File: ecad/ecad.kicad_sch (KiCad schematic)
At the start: 9 parts, among them J1 Raspberry_Pi_2_3, Q1 BC547

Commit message: update schematic
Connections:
- net RFID_IRQ: now reaches J1.18 (GPIO24)
- net RFID_IRQ: now also U4.5 (IRQ)
- net ~{RFID_RST}: now reaches J1.22 (GPIO25)
- net ~{RFID_RST}: now also U4.7 (RST)
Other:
- note removed: "IRQ and RST are connected to the Pi. Need to look it up."
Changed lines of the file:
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@@
   (no_connect (at 207.01 74.93))
   (no_connect (at 54.61 101.6))
+  (wire (pts (xy 115.57 123.19) (xy 116.84 123.19))
+    (stroke (width 0) (type default))
+  )
   (wire (pts (xy 62.23 127) (xy 62.23 104.14))
     (stroke (width 0) (type default))
@@
     (stroke (width 0) (type default))
   )
+  (wire (pts (xy 115.57 128.27) (xy 116.84 128.27))
+    (stroke (width 0) (type default))
+  )
   (wire (pts (xy 44.45 40.64) (xy 48.26 40.64))
     (stroke (width 0) (type default))
@@
     (stroke (width 0) (type default))
   )
+  (wire (pts (xy 110.49 124.46) (xy 115.57 124.46))
+    (stroke (width 0) (type default))
+  )
   (wire (pts (xy 85.09 81.28) (xy 85.09 78.74))
     (stroke (width 0) (type default))
@@
     (stroke (width 0) (type default))
   )
+  (wire (pts (xy 27.94 104.14) (xy 27.94 102.87))
+    (stroke (width 0) (type default))
+  )
   (wire (pts (xy 91.44 151.13) (xy 91.44 157.48))
     (stroke (width 0) (type default))
@@
     (stroke (width 0) (type default))
   )
+  (wire (pts (xy 27.94 102.87) (xy 26.67 102.87))
+    (stroke (width 0) (type default))
+  )
+  (wire (pts (xy 115.57 127) (xy 110.49 127))
+    (stroke (width 0) (type default))
+  )
   (wire (pts (xy 196.85 69.85) (xy 196.85 74.93))
     (stroke (width 0) (type default))
@@
     (stroke (width 0) (type default))
   )
+  (wire (pts (xy 36.83 104.14) (xy 27.94 104.14))
+    (stroke (width 0) (type default))
+  )
   (wire (pts (xy 201.93 68.58) (xy 201.93 67.31))
     (stroke (width 0) (type default))
@@
     (stroke (width 0) (type default))
   )
+  (wire (pts (xy 26.67 106.68) (xy 36.83 106.68))
+    (stroke (width 0) (type default))
+  )
   (wire (pts (xy 48.26 40.64) (xy 48.26 44.45))
     (stroke (width 0) (type default))
   )
+  (wire (pts (xy 115.57 128.27) (xy 115.57 127))
+    (stroke (width 0) (type default))
+  )
   (wire (pts (xy 62.23 40.64) (xy 66.04 40.64))
     (stroke (width 0) (type default))
@@
     (stroke (width 0) (type default))
   )
+  (wire (pts (xy 115.57 124.46) (xy 115.57 123.19))
+    (stroke (width 0) (type default))
+  )
   (wire (pts (xy 30.48 95.25) (xy 30.48 101.6))
     (stroke (width 0) (type default))
@@
   (wire (pts (xy 57.15 109.22) (xy 54.61 109.22))
     (stroke (width 0) (type default))
-  )
-  (text "IRQ and RST are\nconnected to the Pi.\nNeed to look it up."
-    (at 13.97 107.95 0)
-    (effects (font (size 1.27 1.27)) (justify left bottom))
   )
   (text "Probably best to tie these together along\nthe signal path/close to the amp!"
@@
     (effects (font (size 1.27 1.27)) (justify left bottom))
   )
+  (global_label "RFID_IRQ" (shape input) (at 26.67 102.87 180) (fields_autoplaced)
+    (effects (font (size 1.27 1.27)) (justify right))
+    (property "Intersheetrefs" "${INTERSHEET_REFS}" (at 15.2785 102.87 0)
+      (effects (font (size 1.27 1.27)) (justify right) hide)
+    )
+  )
   (global_label "AudioGND" (shape input) (at 227.33 140.97 0) (fields_autoplaced)
     (effects (font (size 1.27 1.27)) (justify left))
@@
     )
   )
+  (global_label "RFID_IRQ" (shape input) (at 116.84 123.19 0) (fields_autoplaced)
+    (effects (font (size 1.27 1.27)) (justify left))
+    (property "Intersheetrefs" "${INTERSHEET_REFS}" (at 128.2315 123.19 0)
+      (effects (font (size 1.27 1.27)) (justify left) hide)
+    )
+  )
+  (global_label "~{RFID_RST}" (shape input) (at 116.84 128.27 0) (fields_autoplaced)
+    (effects (font (size 1.27 1.27)) (justify left))
+    (property "Intersheetrefs" "${INTERSHEET_REFS}" (at 128.4733 128.27 0)
+      (effects (font (size 1.27 1.27)) (justify left) hide)
+    )
+  )
+  (global_label "~{RFID_RST}" (shape input) (at 26.67 106.68 180) (fields_autoplaced)
+    (effects (font (size 1.27 1.27)) (justify right))
+    (property "Intersheetrefs" "${INTERSHEET_REFS}" (at 15.0367 106.68 0)
+      (effects (font (size 1.27 1.27)) (justify right) hide)
+    )
+  )

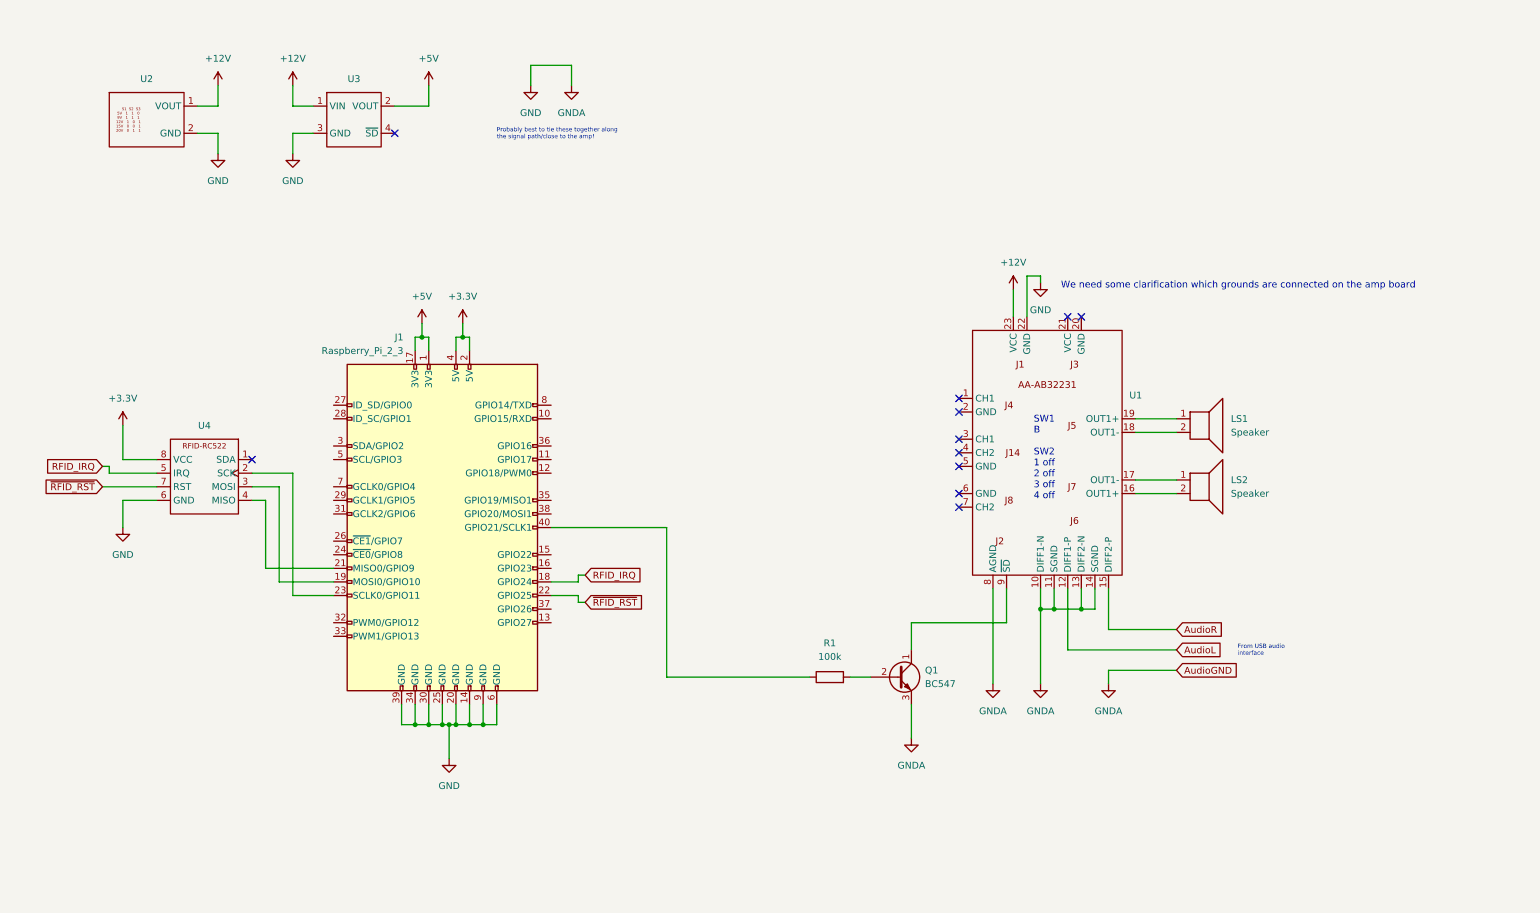
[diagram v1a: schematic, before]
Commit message: pi softoff, new amp power control
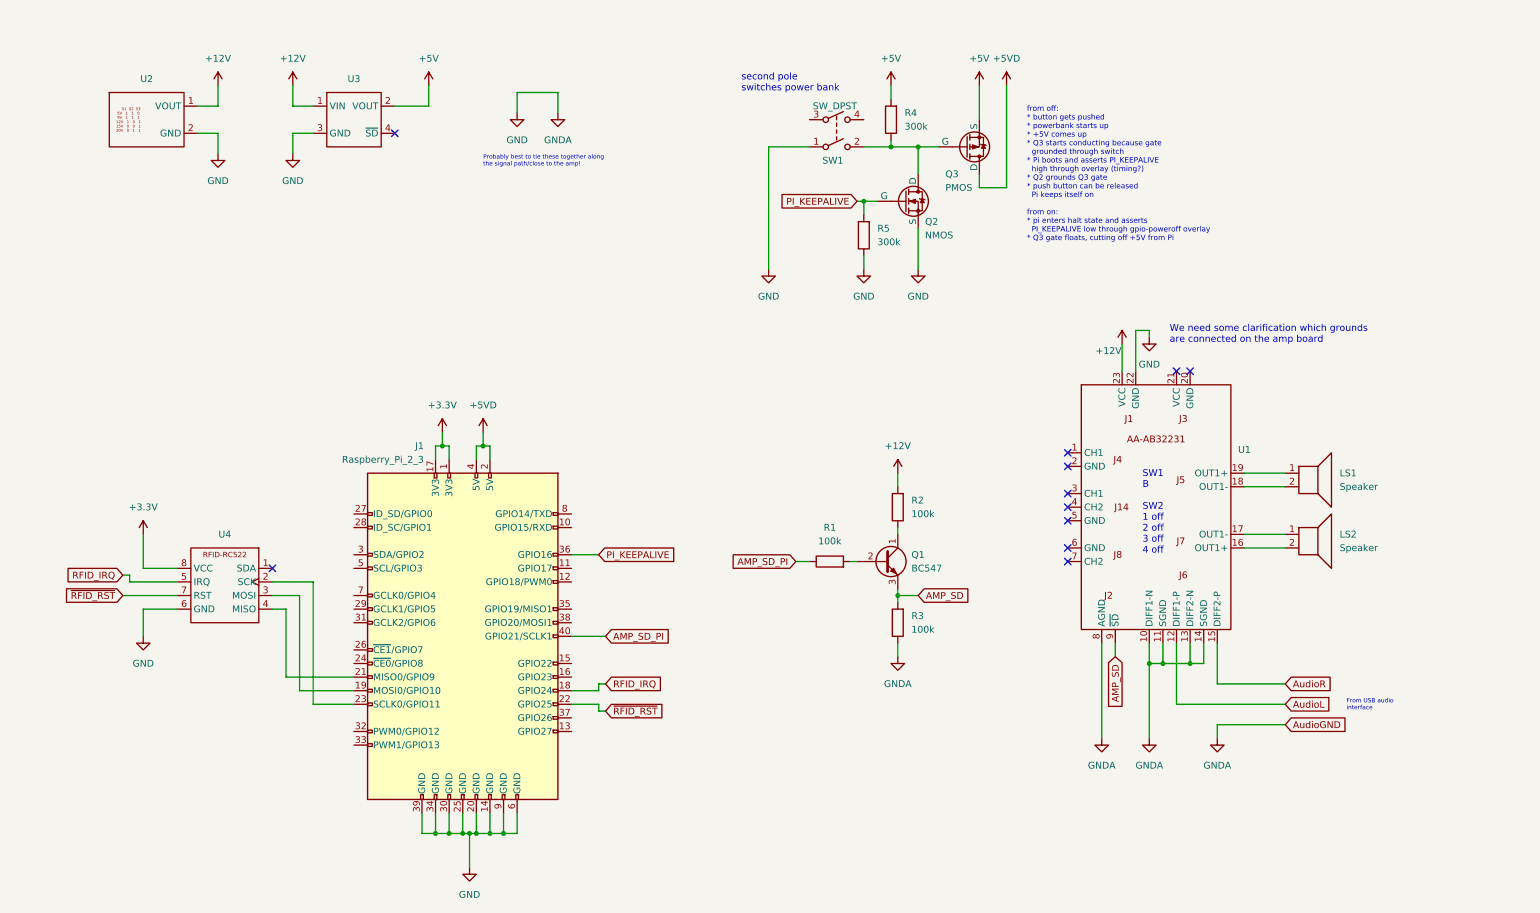
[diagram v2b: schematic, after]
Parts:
- added Q2: NMOS, symbol Simulation_SPICE:NMOS
- added Q3: PMOS, symbol Simulation_SPICE:PMOS
- added R2, R3: 100k, symbol Device:R
- added R4, R5: 300k, symbol Device:R
- added SW1: SW_DPST, symbol Switch:SW_DPST
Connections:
- net +12V: now also R2.2
- net +3.3V: now also J1.1 (3V3), J1.17 (3V3); no longer J1.2 (5V), J1.4 (5V)
- net +5V: now also Q3.3 (S), R4.2; no longer J1.1 (3V3), J1.17 (3V3)
- net GND: now also Q2.3 (S), R3.1, R5.1, SW1.1; no longer Q1.3 (E)
- net PI_KEEPALIVE: now reaches J1.36 (GPIO16)
- net PI_KEEPALIVE: now also Q2.2 (G), R5.2
- net AMP_SD_PI: now reaches J1.40 (GPIO21/SCLK1), R1.1
- net at Q1.1 (C): now also R2.1; no longer U1.9 (~{SD})
- new net: Q2.1 (D), Q3.2 (G), R4.1, SW1.2
- new net +5VD: J1.2 (5V), J1.4 (5V), Q3.1 (D)
- new net AMP_SD: Q1.3 (E), R3.2, U1.9 (~{SD})
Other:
- note added: "from off: * button gets pushed * powerbank starts up * +5V comes up * Q3 starts conducting because gate grounded through switch * Pi boots and asserts PI_KEEPALIVE high through overlay (timing?) * Q2 grounds Q3 gate * push button can be released Pi keeps itself on from on: * pi enters halt state and asserts PI_KEEPALIVE low through gpio-poweroff overlay * Q3 gate floats, cutting off +5V from Pi"
- note added: "second pole switches power bank"
- moved on the sheet: J1, LS1, LS2, Q1, R1, U1, U4

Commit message: updated amp control, more notes
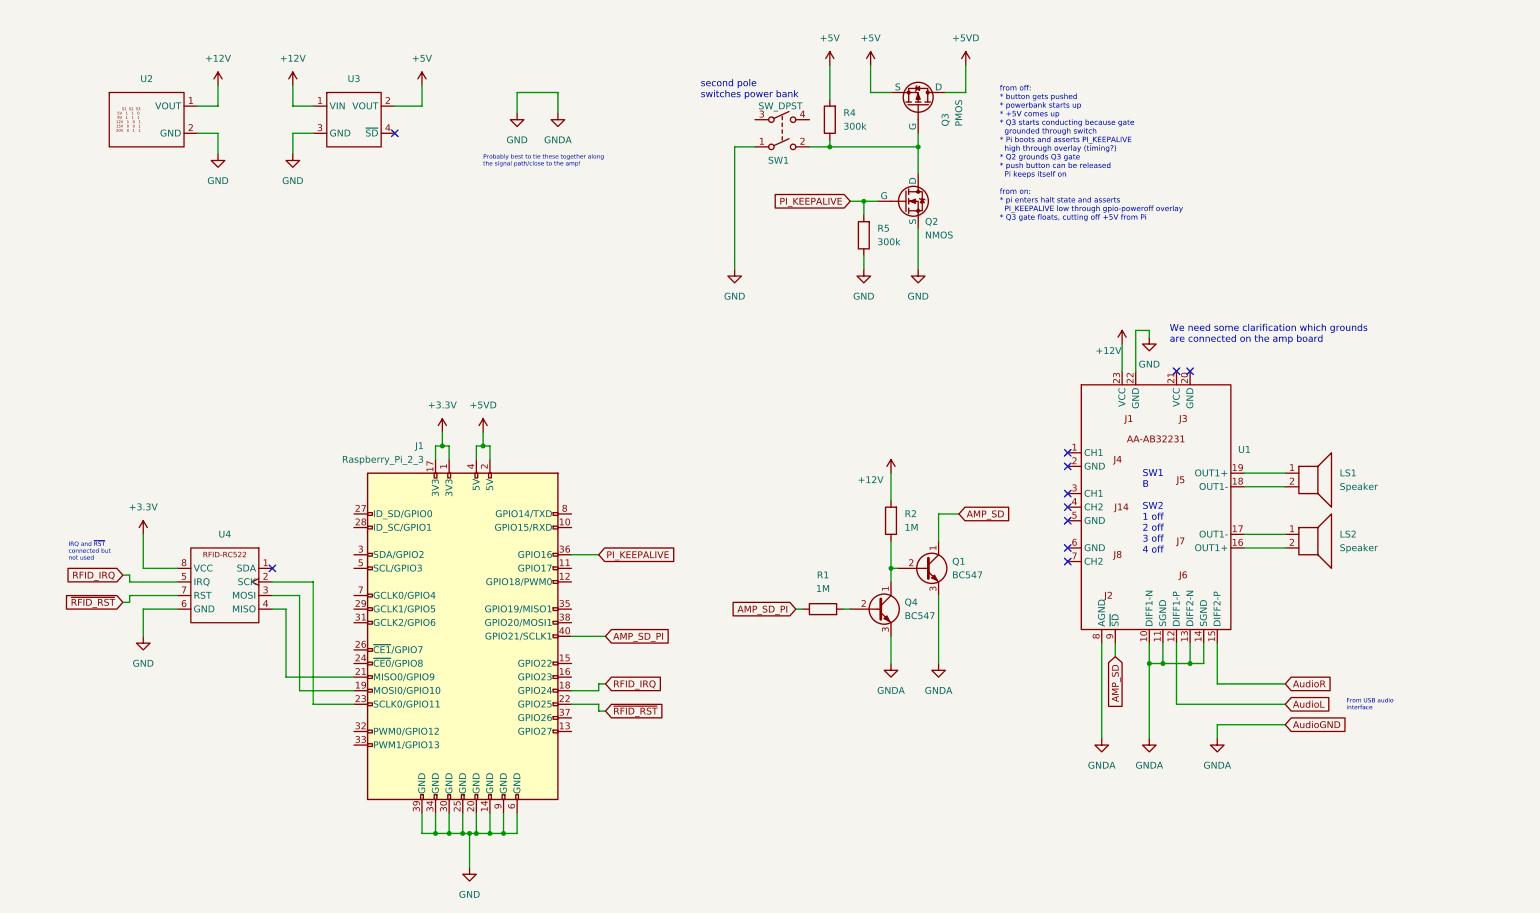
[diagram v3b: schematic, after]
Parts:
- removed R3: 100k, symbol Device:R
- added Q4: BC547, Package_TO_SOT_THT:TO-92_Inline, symbol Transistor_BJT:BC547
- R1, R2: value 100k -> 1M
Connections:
- net AMP_SD: now also Q1.1 (C); no longer Q1.3 (E)
- net GND: now also Q1.3 (E), Q4.3 (E)
- net at R2.1: now also Q1.2 (B), Q4.1 (C); no longer Q1.1 (C)
- net at R1.2: now also Q4.2 (B); no longer Q1.2 (B)
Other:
- note added: "IRQ and ~{RST} connected but not used"
- moved on the sheet: Q1, Q3, R1, R2, R4, SW1

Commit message: refine power management
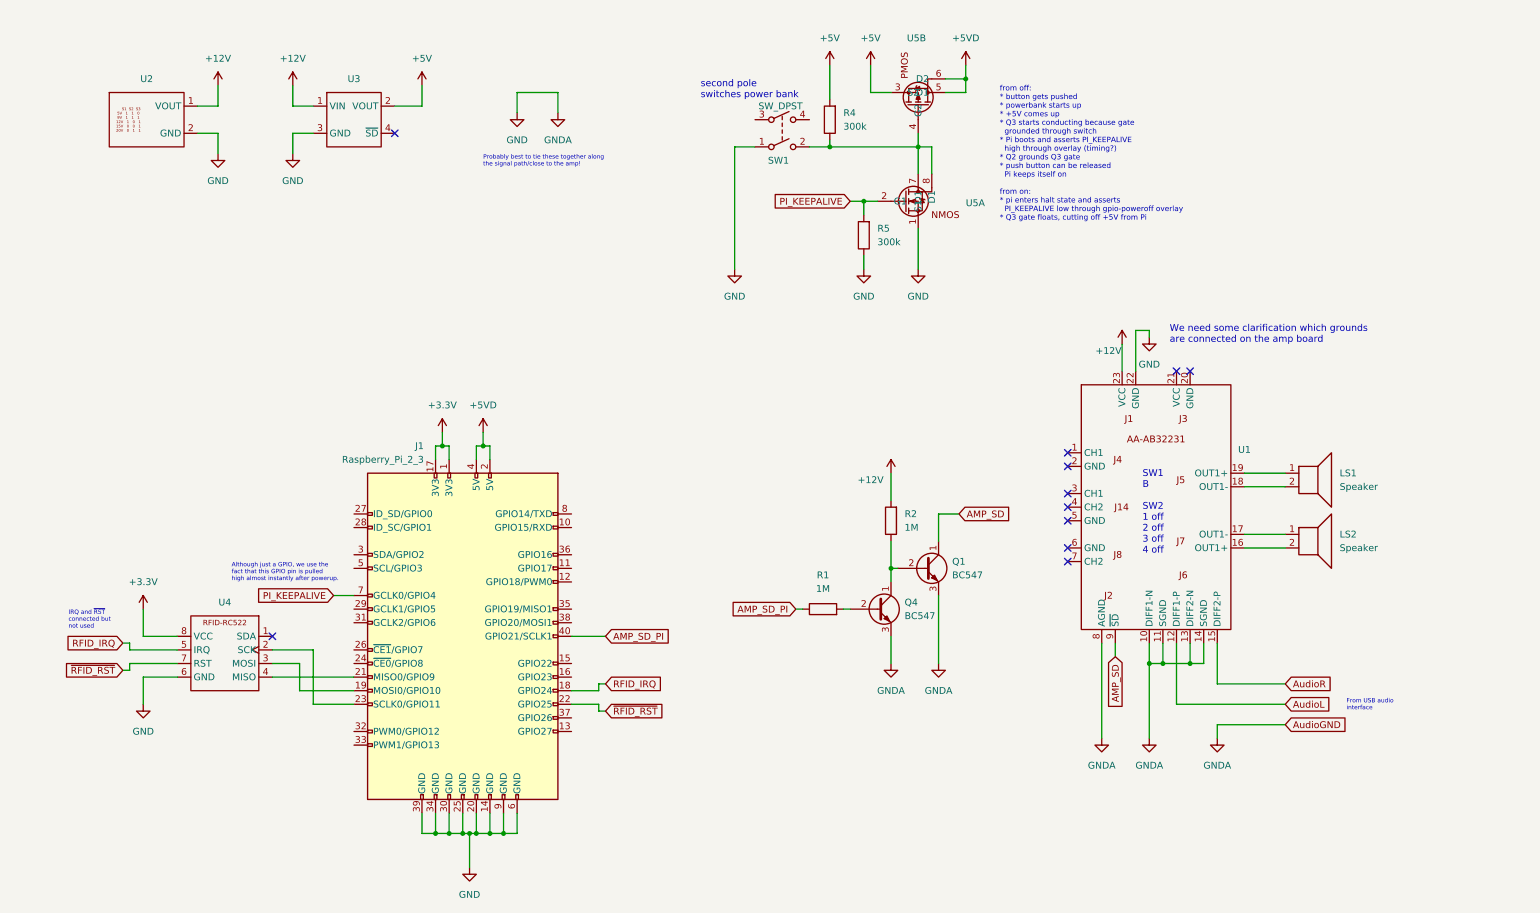
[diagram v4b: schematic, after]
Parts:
- removed Q2: NMOS, symbol Simulation_SPICE:NMOS
- removed Q3: PMOS, symbol Simulation_SPICE:PMOS
- added U5: ~, symbol drempelbox:IRF7319
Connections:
- net +5V: now also U5.3 (S2)
- net +5VD: now also U5.5 (D1), U5.6 (D2)
- net GND: now also U5.1 (S1)
- net PI_KEEPALIVE: now also J1.7 (GCLK0/GPIO4), U5.2 (G1); no longer J1.36 (GPIO16)
- net at R4.1, SW1.2: now also U5.4 (G2), U5.7 (D1), U5.8 (D1)
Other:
- note added: "Although just a GPIO, we use the fact that this GPIO pin is pulled high almost instantly after powerup."
- moved on the sheet: U4

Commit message: add PI shutdown input
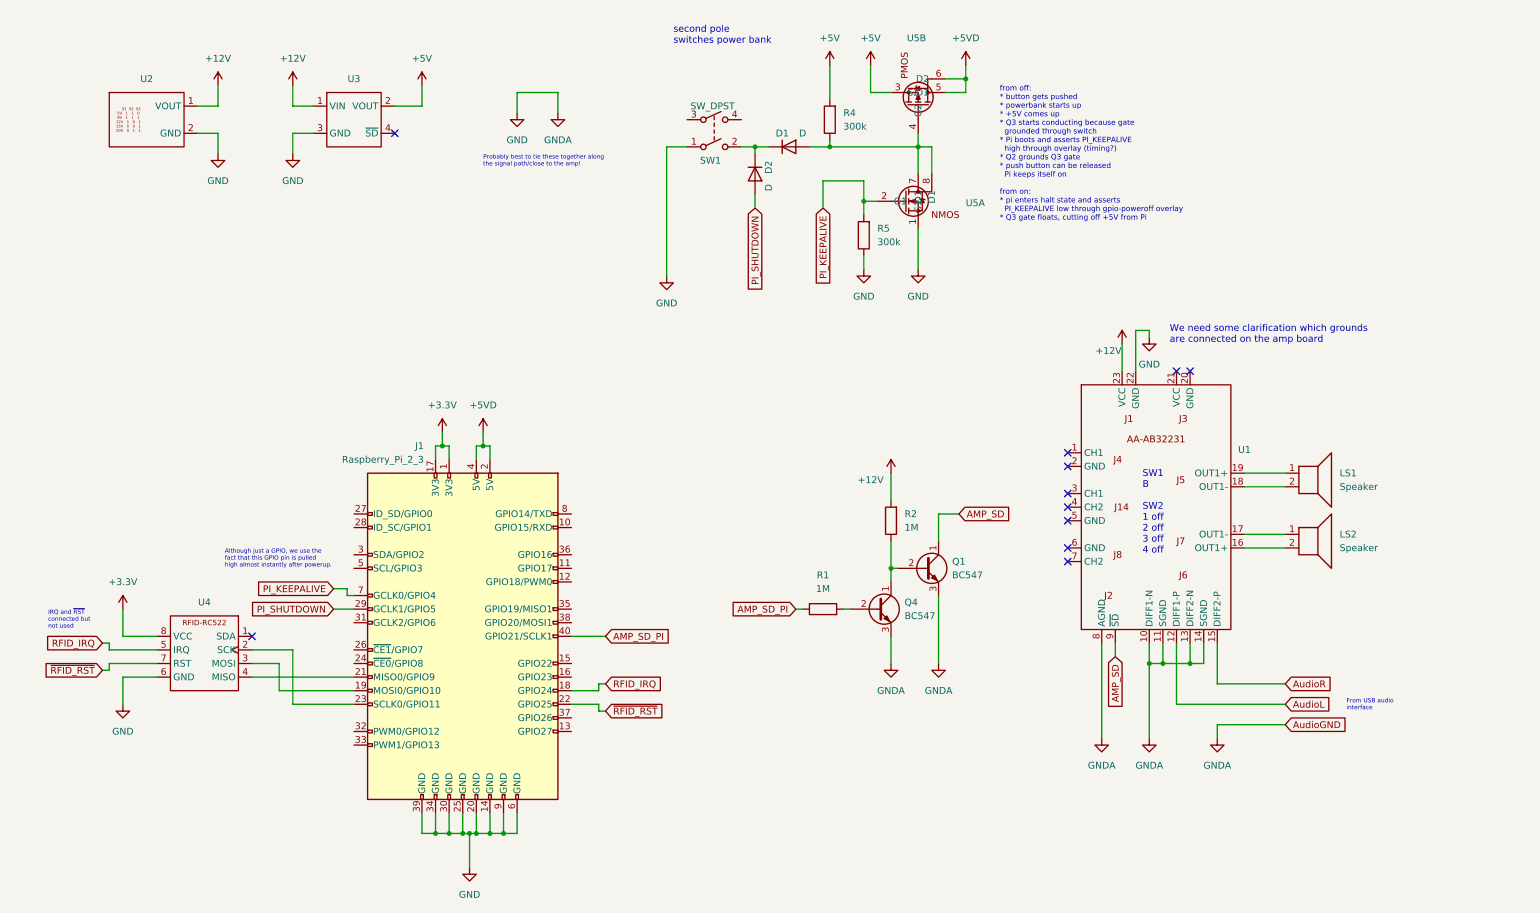
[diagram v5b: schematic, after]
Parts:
- added D1, D2: D, symbol Device:D
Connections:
- net at R4.1, U5.4 (G2), U5.7 (D1)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: now also D1.2 (A); no longer SW1.2
- net PI_SHUTDOWN: now reaches J1.29 (GCLK1/GPIO5)
- net PI_SHUTDOWN: now also D2.2 (A)
- new net: D1.1 (K), D2.1 (K), SW1.2
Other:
- moved on the sheet: SW1, U4
